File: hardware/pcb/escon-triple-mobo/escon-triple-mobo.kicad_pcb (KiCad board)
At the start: 2 copper layers, 160 x 100 mm, 66 parts, among them J1 PHOENIX-COMBICON-MCV-4POS, J2 PHOENIX-COMBICON-MCV-2POS, J3 PHOENIX-COMBICON-MCV-4POS, J4 PHOENIX-COMBICON-MCV-4POS, P1 CONN_02X20, P2 CONN_02X04, P3 CONN_02X04, P4 CONN_02X07

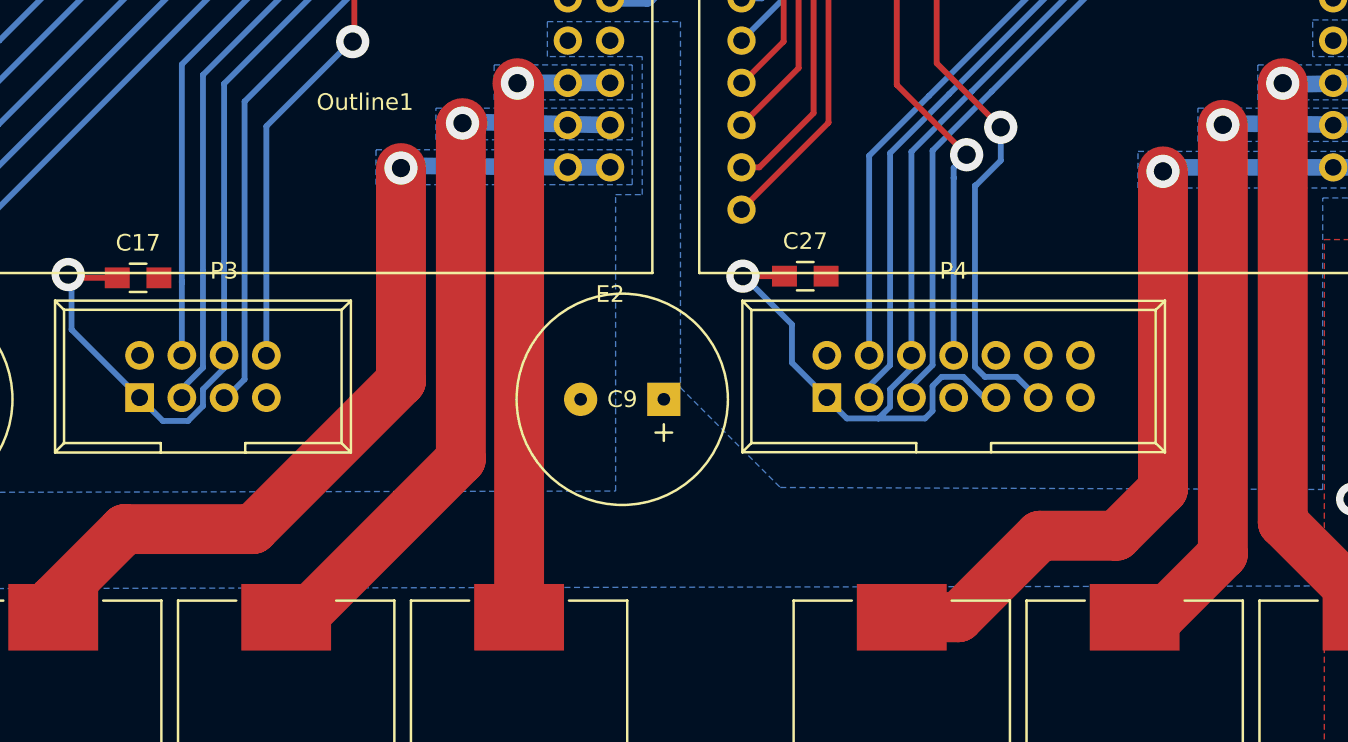
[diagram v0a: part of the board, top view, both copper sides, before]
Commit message: small changes in hardware files. Prolly just metadata. Updated parameter estimation scripts
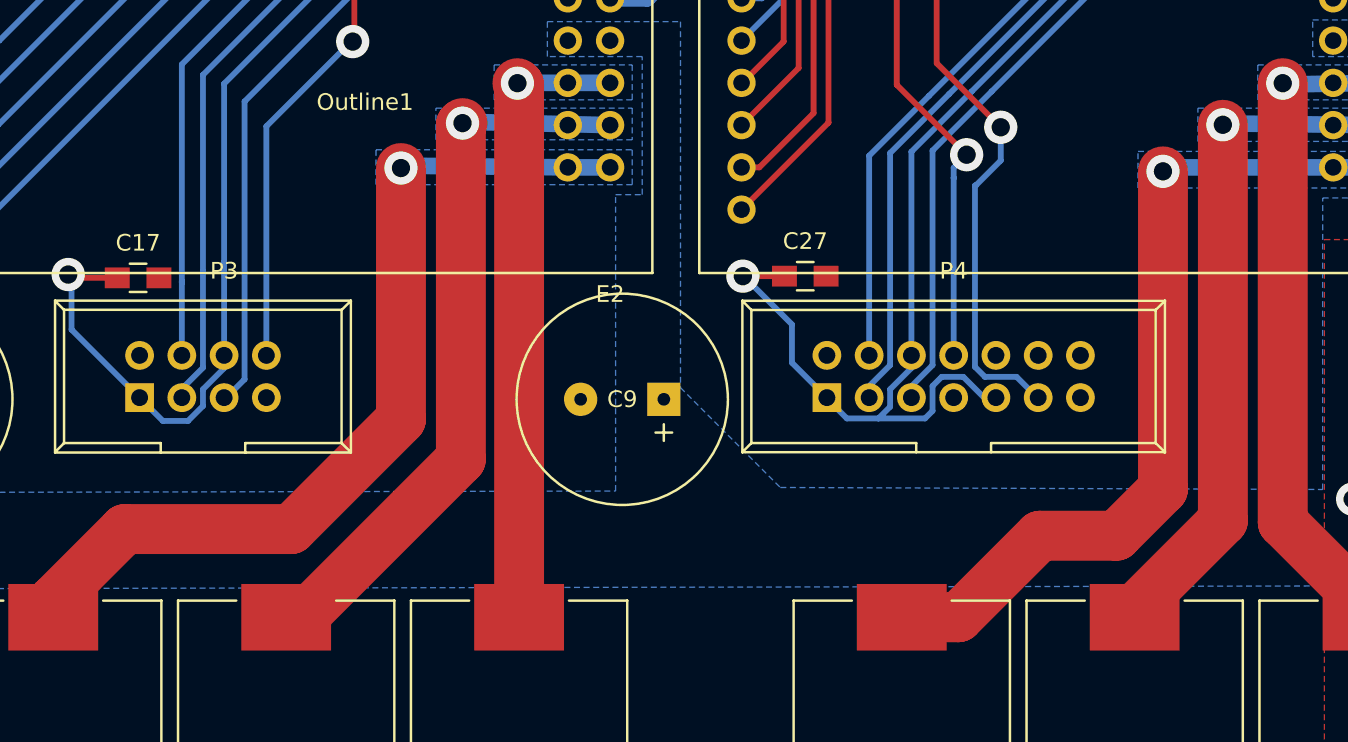
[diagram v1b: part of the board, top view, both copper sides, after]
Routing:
- net Net-(E2-Pad1): track 52.8 -> 54.1 mm
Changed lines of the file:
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@@
     (links 181)
     (no_connects 0)
-    (area 0 0 0 0)
+    (area 33 30 196.700001 134.500001)
     (thickness 1.6)
     (drawings 1)
@@
   (segment (start 95 102) (end 95 101) (width 3) (layer F.Cu) (net 76))
   (segment (start 95 101) (end 99.3 96.7) (width 3) (layer F.Cu) (net 76))
-  (segment (start 99.3 96.7) (end 107 96.7) (width 3) (layer F.Cu) (net 76))
-  (segment (start 107 96.7) (end 115.9 87.8) (width 3) (layer F.Cu) (net 76))
-  (segment (start 115.9 87.8) (end 115.9 75) (width 3) (layer F.Cu) (net 76))
+  (segment (start 99.3 96.7) (end 109.3 96.7) (width 3) (layer F.Cu) (net 76))
+  (segment (start 109.3 96.7) (end 115.9 90.1) (width 3) (layer F.Cu) (net 76))
+  (segment (start 115.9 90.1) (end 115.9 75) (width 3) (layer F.Cu) (net 76))
   (via (at 115.9 75) (size 2) (drill 1.1) (layers F.Cu B.Cu) (net 76))
   (segment (start 115.9 75) (end 116.04 74.86) (width 1) (layer B.Cu) (net 76))
@@
   (segment (start 154.3 97.1) (end 158.9 97.1) (width 3) (layer F.Cu) (net 83))
   (segment (start 149.4 102) (end 154.3 97.1) (width 3) (layer F.Cu) (net 83))
-  (segment (start 160 102) (end 161.5 102) (width 3) (layer F.Cu) (net 84))
-  (segment (start 161.5 102) (end 165.3 98.2) (width 3) (layer F.Cu) (net 84))
-  (segment (start 165.3 98.2) (end 165.3 72.4) (width 3) (layer F.Cu) (net 84))
+  (segment (start 160 102) (end 159.5 102) (width 3) (layer F.Cu) (net 84))
+  (segment (start 159.5 102) (end 165.3 96.2) (width 3) (layer F.Cu) (net 84))
+  (segment (start 165.3 96.2) (end 165.3 72.4) (width 3) (layer F.Cu) (net 84))
   (via (at 165.3 72.4) (size 2) (drill 1.1) (layers F.Cu B.Cu) (net 84))
   (segment (start 165.3 72.4) (end 165.38 72.32) (width 1) (layer B.Cu) (net 84))
